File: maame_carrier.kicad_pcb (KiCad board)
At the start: 2 copper layers, 95 x 110 mm, 26 parts, among them J1 To Kakute H7 V1.5: left strip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, J10 FS-iA10B iBUS servo lead (S +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, J11 TF-Luna pin order 1-6 (CFG ti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, J12 Spare FC I2C (5 V supply, sha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, J13 Payload servo power (+ -); se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, J17 Kakute spare: T3 RSSI 3V3(FC)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, J3 VBAT tap from ESC battery pad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, J4 Micro BEC input leads (6-60 V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, J5 Micro BEC output leads (set t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, J6 Spare power: 5V_AUX G 5V_FC G, J7 Pi expansion: 3V3 logic ONLY, J8 TBS M10Q: order matches its p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, J9 SiK radio (UART4), U1 Raspberry Pi Zero W v1.1, com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

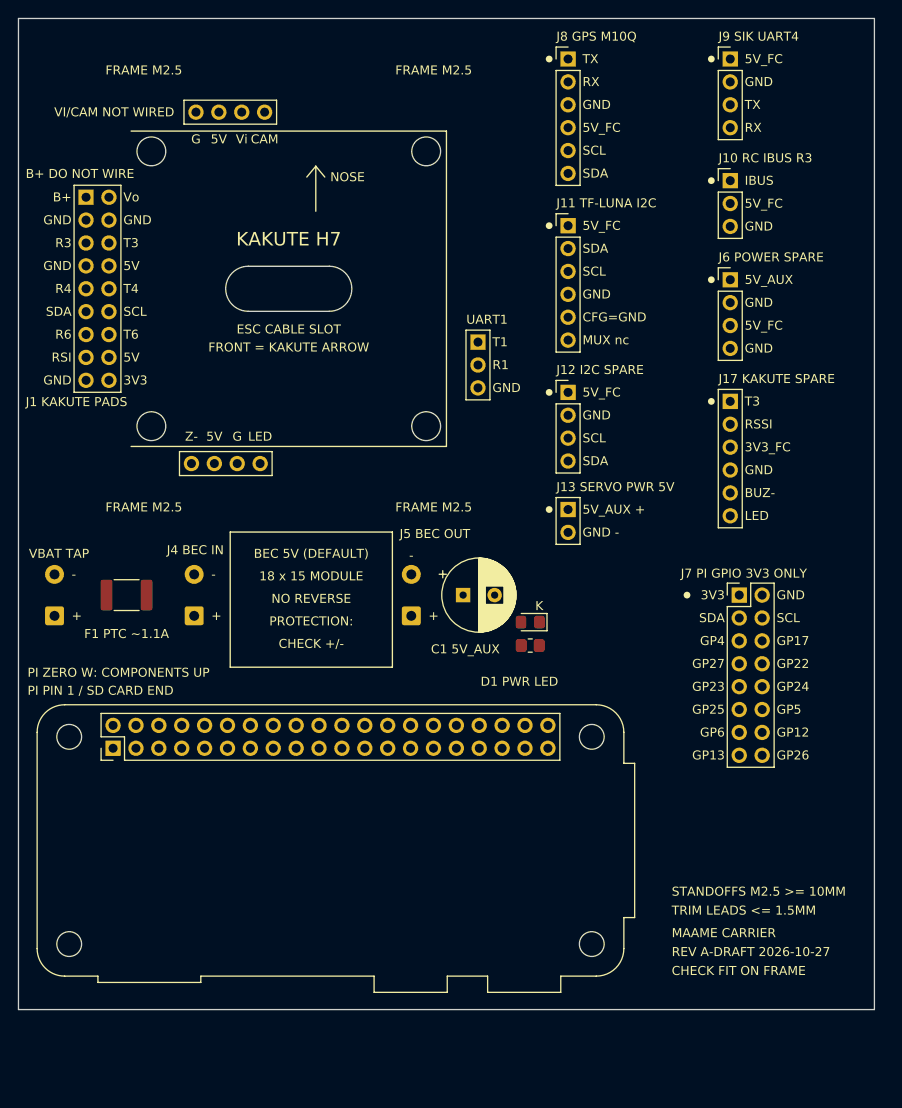
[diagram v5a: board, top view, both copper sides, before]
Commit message: Centre the board on the Kakute: FC = frame-square centre = outline centre (95 x 111); power + J7 front, headers on both sides, Pi across the rear
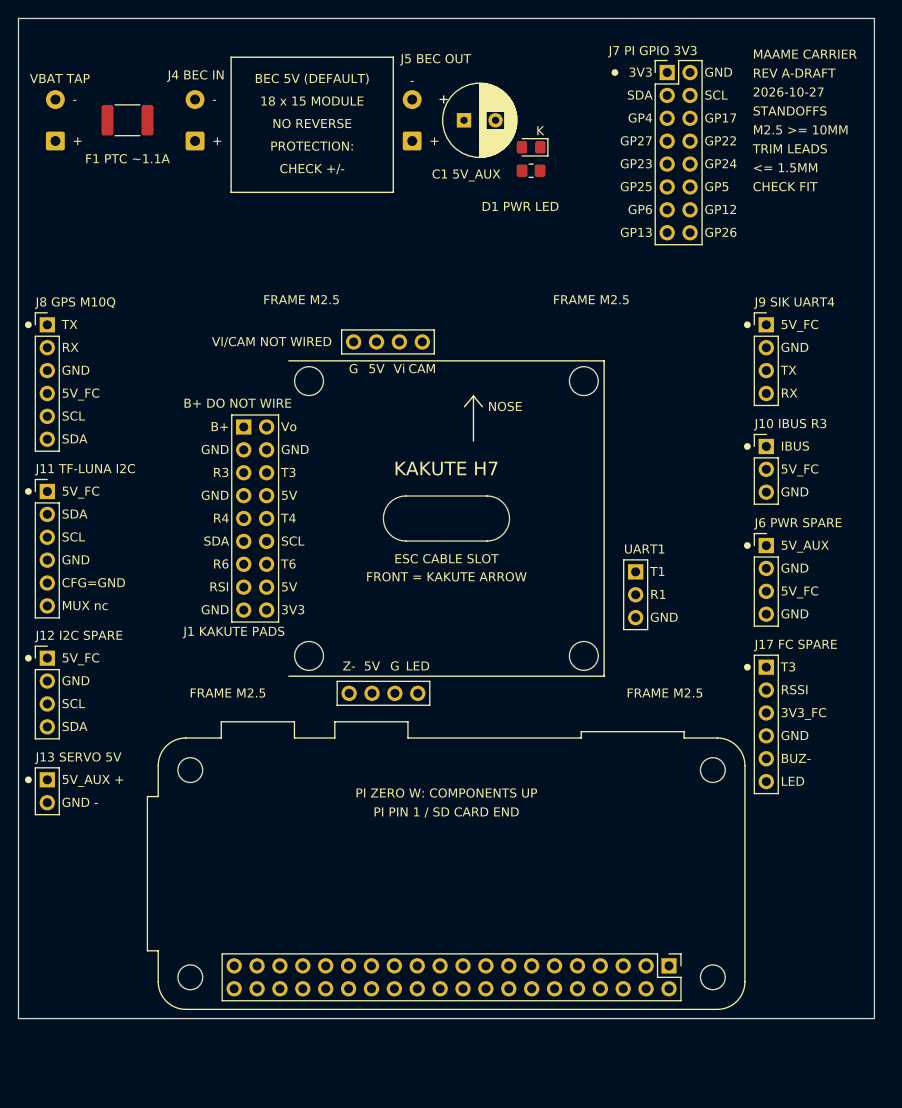
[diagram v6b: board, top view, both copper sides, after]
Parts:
- moved U1 66.3 mm to (72.2, 105.2), turned to 90 degrees
- moved J13 65.1 mm to (3.20, 84.5)
- moved J11 64.9 mm to (3.20, 52.5)
- moved J12 64.9 mm to (3.20, 71.0)
- moved J8 64.9 mm to (3.20, 34.0)
- moved J7 58.5 mm to (72.0, 6.00)
- moved C1 52.7 mm to (49.5, 11.3)
- moved D1 52.7 mm to (56.9, 14.3)
- moved F1 52.7 mm to (12.1, 11.3)
- moved J3 52.7 mm to (4.10, 13.6)
- moved J4 52.7 mm to (19.6, 13.6)
- moved J5 52.7 mm to (43.7, 13.6)
- moved R1 52.7 mm to (56.9, 16.9)
- moved H1 30.9 mm to (32.2, 40.2)
- moved H2 30.9 mm to (62.8, 40.2)
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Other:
- board size 95 x 110 mm -> 95 x 111 mm
- board text added: "2026-10-27"
- board text added: "<= 1.5MM"
- board text added: "CHECK FIT"
- board text added: "J10 IBUS R3"
- board text added: "J13 SERVO 5V"
- board text added: "J17 FC SPARE"
- board text added: "J6 PWR SPARE"
- board text added: "J7 PI GPIO 3V3"
- board text added: "M2.5 >= 10MM"
- board text added: "REV A-DRAFT"
- board text added: "STANDOFFS"
- board text added: "TRIM LEADS"
- board text removed: "CHECK FIT ON FRAME"
- board text removed: "J10 RC IBUS R3"
- board text removed: "J13 SERVO PWR 5V"
- board text removed: "J17 KAKUTE SPARE"
- board text removed: "J6 POWER SPARE"
- board text removed: "J7 PI GPIO 3V3 ONLY"
- board text removed: "REV A-DRAFT 2026-10-27"
- board text removed: "STANDOFFS M2.5 >= 10MM"
- board text removed: "TRIM LEADS <= 1.5MM"

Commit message: Pi turned so USB/HDMI overhang the rear edge; rear frame screws clear of the Pi; board 95 x 116.5, still centred on the Kakute
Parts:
- moved U1 51.2 mm to (22.8, 91.8), turned to 270 degrees
- moved J3 2.75 mm to (4.10, 16.4)
- moved J4 2.75 mm to (19.6, 16.4)
- moved J5 2.75 mm to (43.7, 16.4)
- moved C1 2.75 mm to (49.5, 14.1)
- moved D1 2.75 mm to (56.9, 17.1)
- moved F1 2.75 mm to (12.1, 14.1)
- moved H1 2.75 mm to (32.2, 43.0)
- moved H2 2.75 mm to (62.8, 43.0)
- moved H3 2.75 mm to (32.2, 73.5)
- moved H4 2.75 mm to (62.8, 73.5)
- moved H5 2.75 mm to (23.2, 34.0)
- moved H6 2.75 mm to (71.8, 34.0)
- moved H7 2.75 mm to (23.2, 82.5)
- moved H8 2.75 mm to (71.8, 82.5)
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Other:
- board size 95 x 111 mm -> 95 x 116.5 mm
- board text added: "PIN 1 + SD CARD: LEFT END"
- board text added: "USB / HDMI: REAR EDGE"
- board text removed: "PI PIN 1 / SD CARD END"

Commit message: Rounded 3 mm corners; status LED row: FC5V, AUX5V (hardware), PI/DATA/BATT H-M-L on Pi GPIO16/20/19/21/18
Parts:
- added D2: Green 0805: 5V_FC on, LED_SMD:LED_0805_2012Metric_Pad1.15x1.40mm_HandSolder, F.Cu at (29.0, 27.5)
- added D3: Green 0805: Pi active (GPIO16), LED_SMD:LED_0805_2012Metric_Pad1.15x1.40mm_HandSolder, F.Cu at (40.0, 27.5)
- added D4: Yellow 0805: data (GPIO20), LED_SMD:LED_0805_2012Metric_Pad1.15x1.40mm_HandSolder, F.Cu at (45.5, 27.5)
- added D5: Green 0805: battery high (GPIO19), LED_SMD:LED_0805_2012Metric_Pad1.15x1.40mm_HandSolder, F.Cu at (51.0, 27.5)
- added D6: Yellow 0805: battery mid (GPIO21), LED_SMD:LED_0805_2012Metric_Pad1.15x1.40mm_HandSolder, F.Cu at (56.5, 27.5)
- added D7: Red 0805: battery low (GPIO18), LED_SMD:LED_0805_2012Metric_Pad1.15x1.40mm_HandSolder, F.Cu at (62.0, 27.5)
- added R2: 1k 0805, Resistor_SMD:R_0805_2012Metric_Pad1.20x1.40mm_HandSolder, F.Cu at (29.0, 30.6)
- added R3: 330R 0805, Resistor_SMD:R_0805_2012Metric_Pad1.20x1.40mm_HandSolder, F.Cu at (40.0, 30.6)
- added R4: 330R 0805, Resistor_SMD:R_0805_2012Metric_Pad1.20x1.40mm_HandSolder, F.Cu at (45.5, 30.6)
- added R5: 330R 0805, Resistor_SMD:R_0805_2012Metric_Pad1.20x1.40mm_HandSolder, F.Cu at (51.0, 30.6)
- added R6: 330R 0805, Resistor_SMD:R_0805_2012Metric_Pad1.20x1.40mm_HandSolder, F.Cu at (56.5, 30.6)
- added R7: 390R 0805, Resistor_SMD:R_0805_2012Metric_Pad1.20x1.40mm_HandSolder, F.Cu at (62.0, 30.6)
- moved R1 24.9 mm to (34.5, 30.6)
- moved D1 24.7 mm to (34.5, 27.5), turned to 0 degrees
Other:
- outline, holes or cut-outs redrawn
- board text added: "AUX5V"
- board text added: "B-H"
- board text added: "B-L"
- board text added: "B-M"
- board text added: "DATA"
- board text added: "FC5V"
- board text added: "PI"
- board text added: "STATUS"
- board text removed: "D1 PWR LED"
- board text removed: "K"
